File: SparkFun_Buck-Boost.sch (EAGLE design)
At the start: 32 parts, among them U1 TPS63070

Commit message: v10
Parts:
- added C9: 10uF, SparkFun-Capacitors:10UF-0805-25V-10%
- added J3: (no value), SparkFun-Connectors:CONN_07NO_SILK
- added R7: 10k, SparkFun-Resistors:10KOHM-0603-1/10W-1%
- FD1, FD2, FD3, FD4: value FIDUCIAL1X2 -> FIDUCIALUFIDUCIAL; device SparkFun-Aesthetics:FIDUCIAL1X2 -> SparkFun-Aesthetics:FIDUCIALUFIDUCIAL
- R5: value 698k -> CUSTOM; device SparkFun-Resistors:698KOHM -> SparkFun-Resistors:RESISTORAXIAL-0.3
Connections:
- removed net N$3: R1.1, U1.!EN, U1.PS/SYNC
- new net !EN: J3.6, R1.1, U1.!EN
- new net PG: J3.2, U1.PG
- new net PS: J3.4, R7.1, U1.PS/SYNC
- net GND: now also C9.2, J3.3, J3.5
- net VIN: now also C9.1, J3.7, R7.2
- net VOUT: now also J3.1
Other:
- note added: "3V3"
- note added: "5V0"
- note added: "VIN: 3-16V"
- note added: "v10"
- note removed: "VIN: 2-16V"
- note removed: "v01"
- moved on the sheet: C1, C2, C3, C5, C6, C7, C8

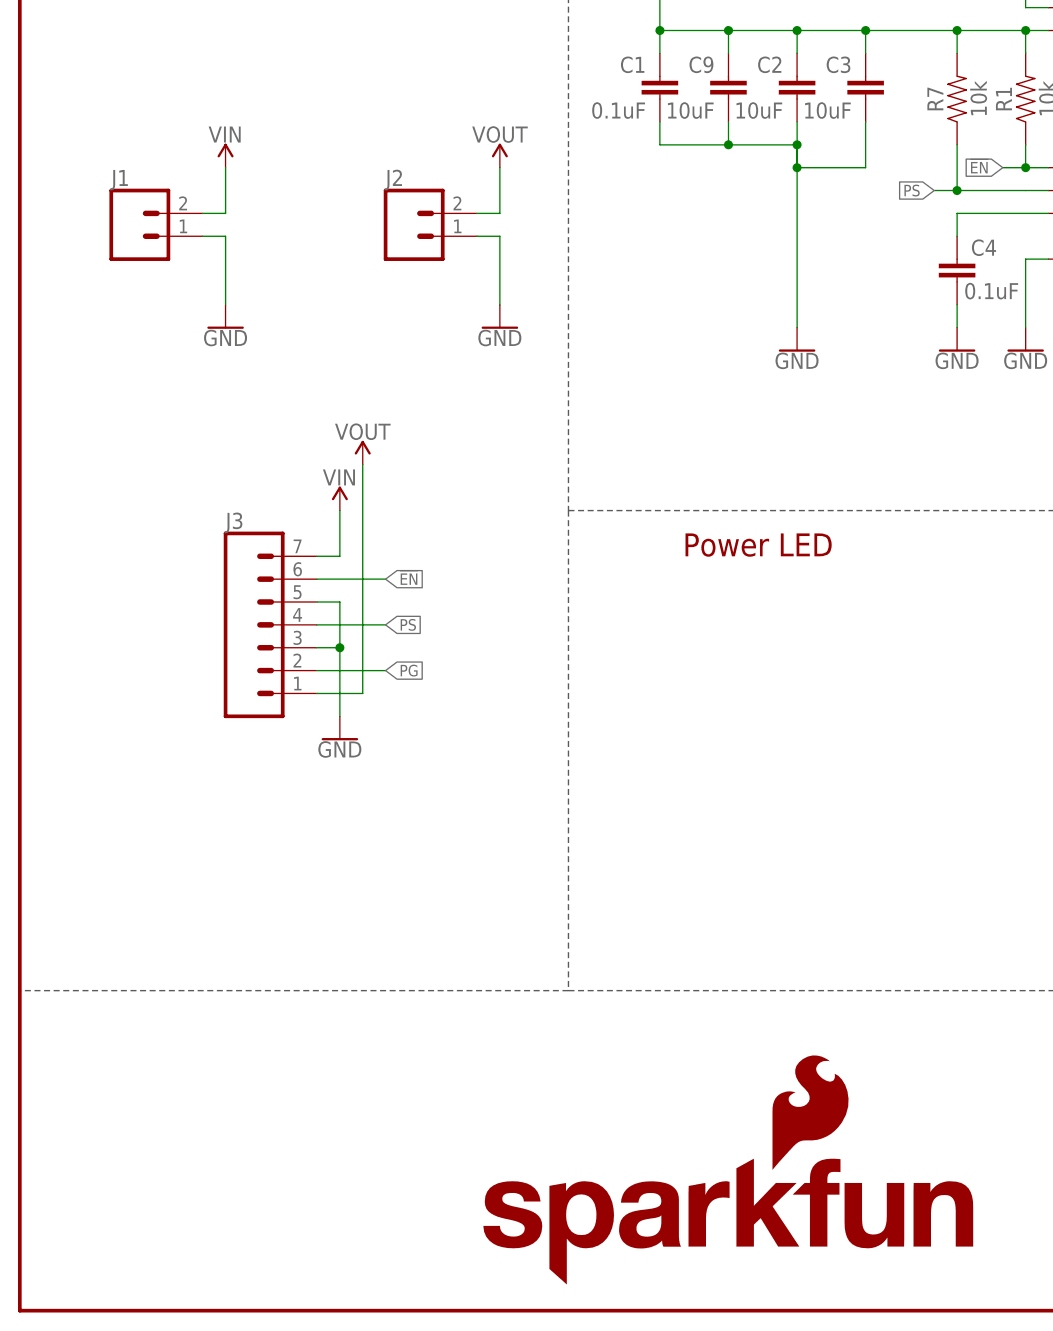
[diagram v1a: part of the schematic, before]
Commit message: V10 changes
- Added note for 2oz copper
- Replace power connections with 3.5mm screw terminals
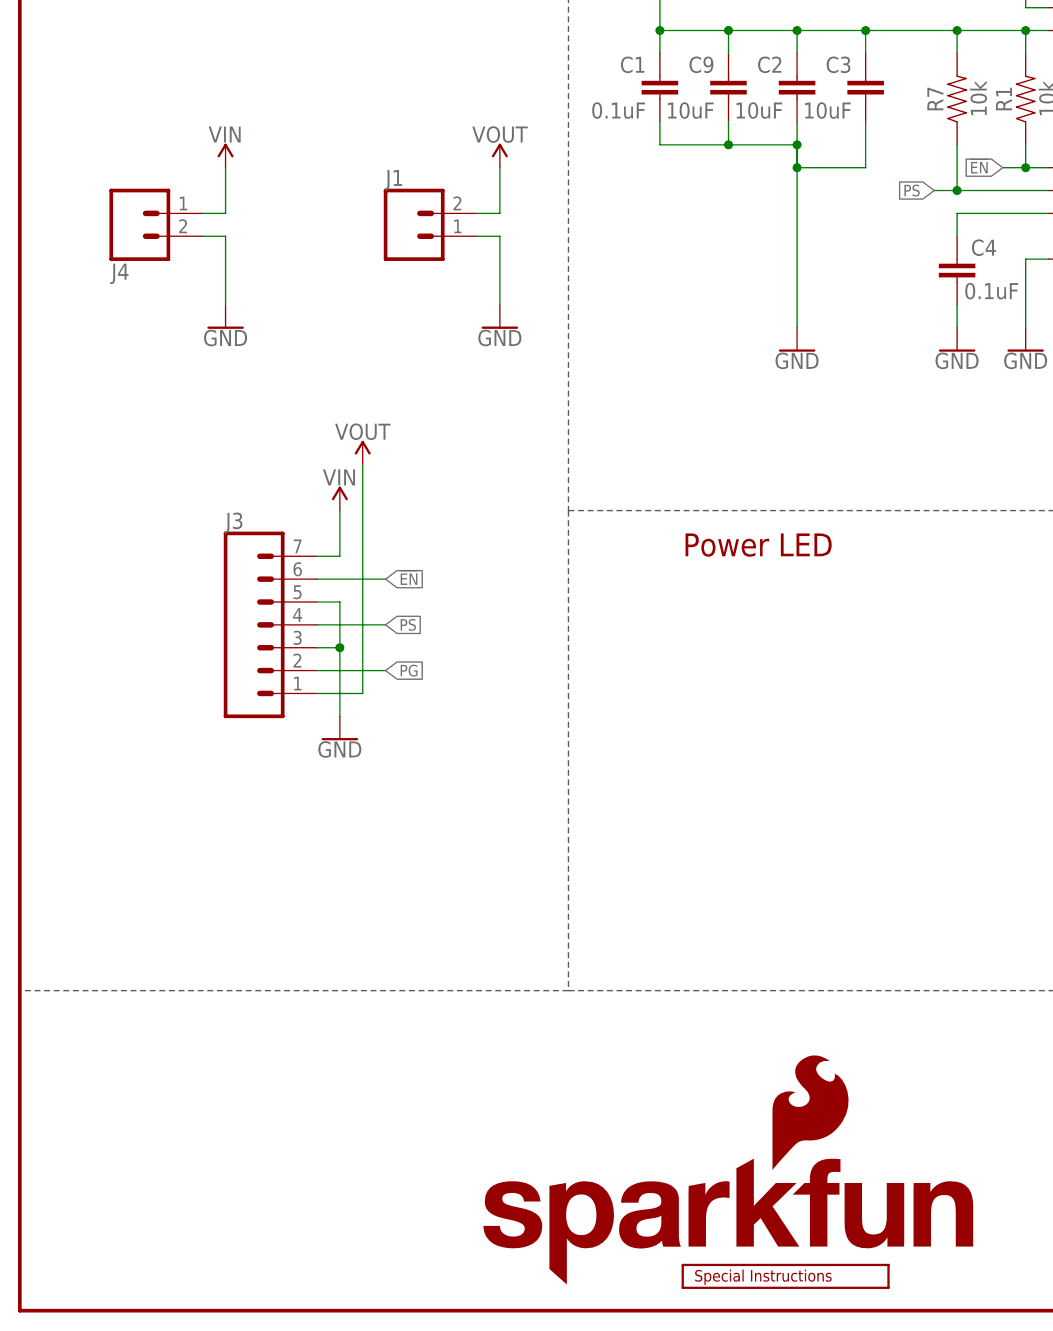
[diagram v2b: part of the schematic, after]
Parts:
- removed J2: (no value), SparkFun-Connectors:CONN_021X02_NO_SILK
- added J4: (no value), SparkFun-Connectors:CONN_023.5MM-NO_SILK
- added LOGO3: SPECIAL_INSTRUCTIONS-ORDERING, SparkFun-Aesthetics:SPECIAL_INSTRUCTIONS-ORDERING
- J1: device SparkFun-Connectors:CONN_021X02_NO_SILK -> SparkFun-Connectors:CONN_023.5MM-NO_SILK
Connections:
- net GND: now also J4.2; no longer J2.1
- net VIN: now also J4.1; no longer J1.2
- net VOUT: now also J1.2; no longer J2.2
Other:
- moved on the sheet: J1
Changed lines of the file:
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@@
 <part name="C1" library="SparkFun-Capacitors" deviceset="0.1UF" device="-0603-25V-(+80/-20%)" value="0.1uF"/>
 <part name="C5" library="SparkFun-Capacitors" deviceset="10UF" device="-0805-25V-10%" value="10uF"/>
-<part name="J1" library="SparkFun-Connectors" deviceset="CONN_02" device="1X02_NO_SILK"/>
-<part name="J2" library="SparkFun-Connectors" deviceset="CONN_02" device="1X02_NO_SILK"/>
 <part name="SUPPLY2" library="SparkFun-PowerSymbols" deviceset="VOUT" device=""/>
 <part name="SUPPLY1" library="SparkFun-PowerSymbols" deviceset="VIN" device=""/>
@@
 <part name="SUPPLY8" library="SparkFun-PowerSymbols" deviceset="VOUT" device=""/>
 <part name="GND8" library="SparkFun-PowerSymbols" deviceset="GND" device=""/>
+<part name="J4" library="SparkFun-Connectors" deviceset="CONN_02" device="3.5MM-NO_SILK"/>
+<part name="J1" library="SparkFun-Connectors" deviceset="CONN_02" device="3.5MM-NO_SILK"/>
+<part name="LOGO3" library="SparkFun-Aesthetics" deviceset="SPECIAL_INSTRUCTIONS" device="-ORDERING"/>
 </parts>
 <sheets>
@@
 <attribute name="VALUE" x="156.464" y="129.921" size="1.778" layer="96" font="vector"/>
 </instance>
-<instance part="J1" gate="G$1" x="12.7" y="119.38" smashed="yes">
-<attribute name="VALUE" x="10.16" y="114.554" size="1.778" layer="96" font="vector"/>
-<attribute name="NAME" x="10.16" y="124.968" size="1.778" layer="95" font="vector"/>
-</instance>
-<instance part="J2" gate="G$1" x="43.18" y="119.38" smashed="yes">
-<attribute name="VALUE" x="40.64" y="114.554" size="1.778" layer="96" font="vector"/>
-<attribute name="NAME" x="40.64" y="124.968" size="1.778" layer="95" font="vector"/>
-</instance>
 <instance part="SUPPLY2" gate="G$1" x="53.34" y="127" smashed="yes">
 <attribute name="VALUE" x="53.34" y="129.794" size="1.778" layer="96" align="bottom-center"/>
@@
 <attribute name="VALUE" x="35.56" y="63.246" size="1.778" layer="96" align="top-center"/>
 </instance>
+<instance part="J4" gate="G$1" x="12.7" y="121.92" rot="MR180"/>
+<instance part="J1" gate="G$1" x="43.18" y="119.38"/>
+<instance part="LOGO3" gate="G$1" x="73.66" y="2.54"/>
 </instances>
 <busses>
@@
 </segment>
 <segment>
-<pinref part="J1" gate="G$1" pin="2"/>
-<wire x1="20.32" y1="121.92" x2="22.86" y2="121.92" width="0.1524" layer="91"/>
 <wire x1="22.86" y1="121.92" x2="22.86" y2="127" width="0.1524" layer="91"/>
 <pinref part="SUPPLY1" gate="G$1" pin="VIN"/>
+<wire x1="20.32" y1="121.92" x2="22.86" y2="121.92" width="0.1524" layer="91"/>
+<pinref part="J4" gate="G$1" pin="1"/>
 </segment>
 <segment>
@@
 </segment>
 <segment>
-<pinref part="J1" gate="G$1" pin="1"/>
-<wire x1="20.32" y1="119.38" x2="22.86" y2="119.38" width="0.1524" layer="91"/>
 <wire x1="22.86" y1="119.38" x2="22.86" y2="111.76" width="0.1524" layer="91"/>
 <pinref part="GND1" gate="1" pin="GND"/>
-</segment>
-<segment>
-<pinref part="J2" gate="G$1" pin="1"/>
-<wire x1="50.8" y1="119.38" x2="53.34" y2="119.38" width="0.1524" layer="91"/>
+<wire x1="20.32" y1="119.38" x2="22.86" y2="119.38" width="0.1524" layer="91"/>
+<pinref part="J4" gate="G$1" pin="2"/>
+</segment>
+<segment>
 <wire x1="53.34" y1="119.38" x2="53.34" y2="111.76" width="0.1524" layer="91"/>
 <pinref part="GND2" gate="1" pin="GND"/>
+<wire x1="50.8" y1="119.38" x2="53.34" y2="119.38" width="0.1524" layer="91"/>
+<pinref part="J1" gate="G$1" pin="1"/>
 </segment>
 <segment>
@@
 </segment>
 <segment>
-<pinref part="J2" gate="G$1" pin="2"/>
-<wire x1="50.8" y1="121.92" x2="53.34" y2="121.92" width="0.1524" layer="91"/>
 <wire x1="53.34" y1="121.92" x2="53.34" y2="127" width="0.1524" layer="91"/>
 <pinref part="SUPPLY2" gate="G$1" pin="VOUT"/>
-</segment>
-<segment>
+<wire x1="50.8" y1="121.92" x2="53.34" y2="121.92" width="0.1524" layer="91"/>
+<pinref part="J1" gate="G$1" pin="2"/>
+</segment>
+<segment>

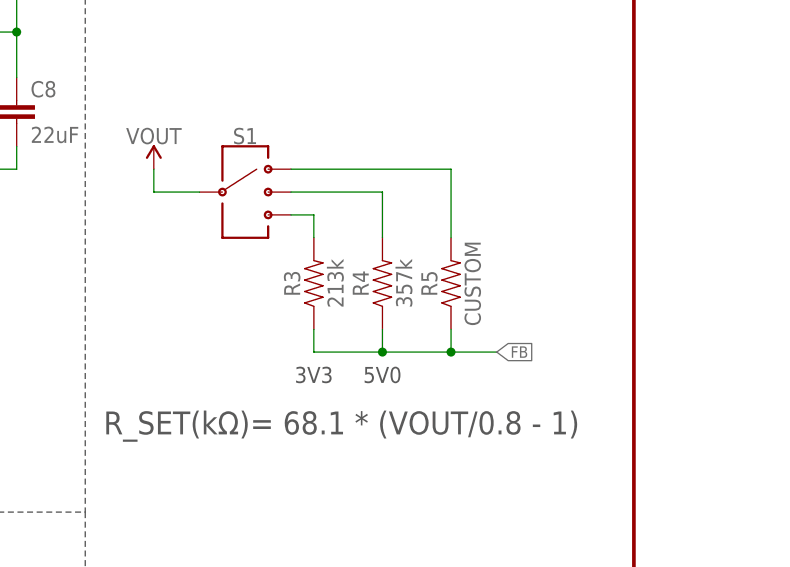
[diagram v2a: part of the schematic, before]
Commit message: Updated BOM
Replaced 357k resistor with 365k resistor
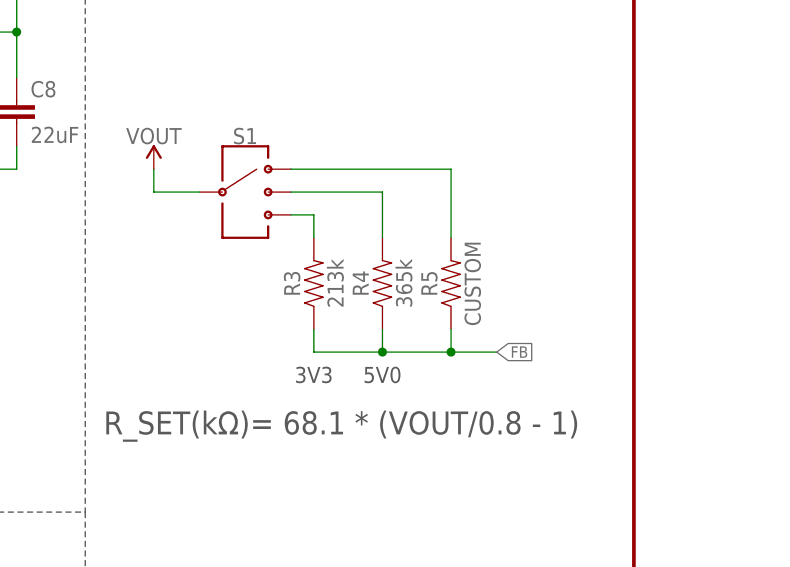
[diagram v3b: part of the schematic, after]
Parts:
- R3: device SparkFun-Resistors:213KOHM -> SparkFun-Resistors:213KOHM-0603-1/10W-0.1%
- R4: value 357k -> 365k; device SparkFun-Resistors:357KOHM -> SparkFun-Resistors:365KOHM-0603-1/10W-1%
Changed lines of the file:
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@@
 <part name="GND2" library="SparkFun-PowerSymbols" deviceset="GND" device=""/>
 <part name="S1" library="SparkFun-Switches" deviceset="SWITCH-SP3T" device="-SMD"/>
-<part name="R3" library="SparkFun-Resistors" deviceset="213KOHM" device="" value="213k"/>
-<part name="R4" library="SparkFun-Resistors" deviceset="357KOHM" device="" value="357k"/>
+<part name="R3" library="SparkFun-Resistors" deviceset="213KOHM" device="-0603-1/10W-0.1%" value="213k"/>
+<part name="R4" library="SparkFun-Resistors" deviceset="365KOHM" device="-0603-1/10W-1%" value="365k"/>
 <part name="R5" library="SparkFun-Resistors" deviceset="RESISTOR" device="AXIAL-0.3" value="CUSTOM"/>
 <part name="H3" library="SparkFun-Hardware" deviceset="STAND-OFF" device=""/>
